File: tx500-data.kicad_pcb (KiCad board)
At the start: 2 copper layers, 80 x 50 mm, 27 parts, among them IC1 HS-100B, J1 USB_B, J2 CAT, J3 REM/DATA, J4 USB_A, U1 TUSB4041I, U2 FT232RL, Y1 24 MHz

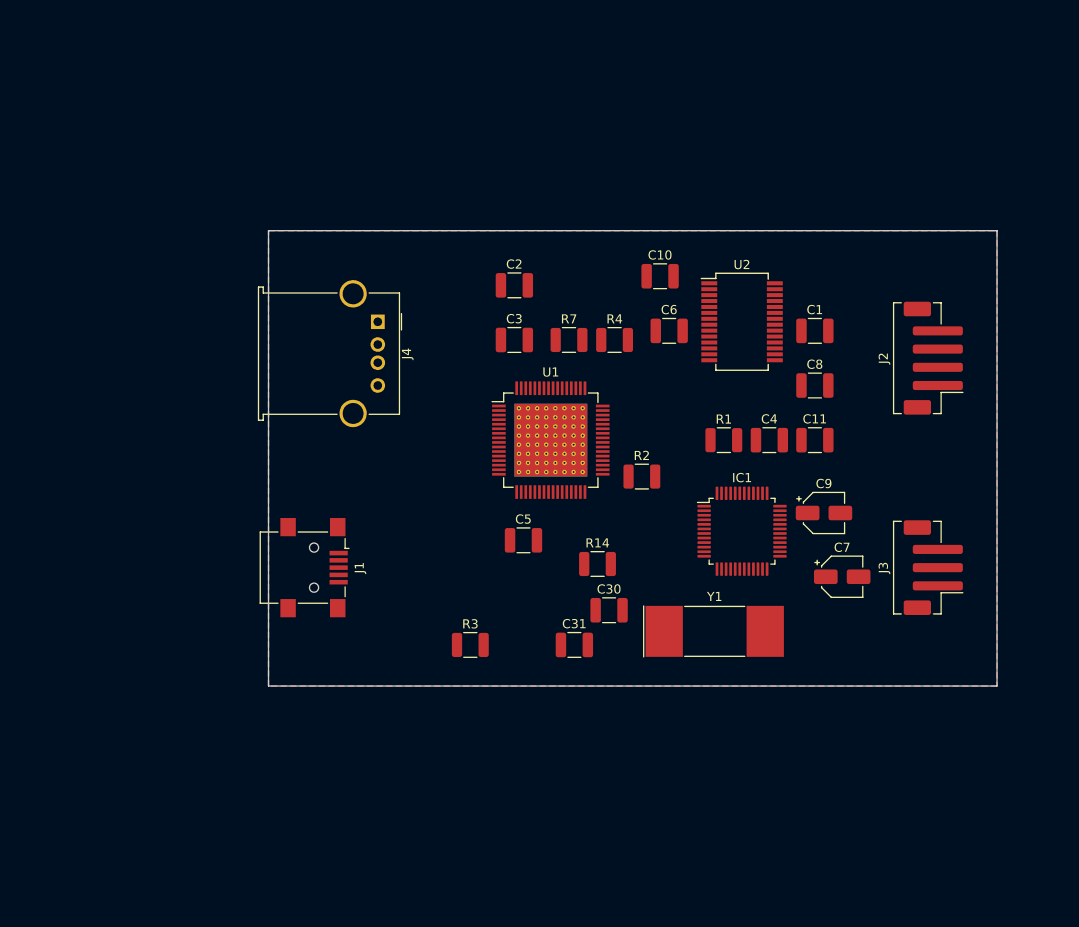
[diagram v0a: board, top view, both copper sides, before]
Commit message: Swap TUSB4041I for TUSB2036
The 4041 does more than I need it to, so use the 2036 instead.
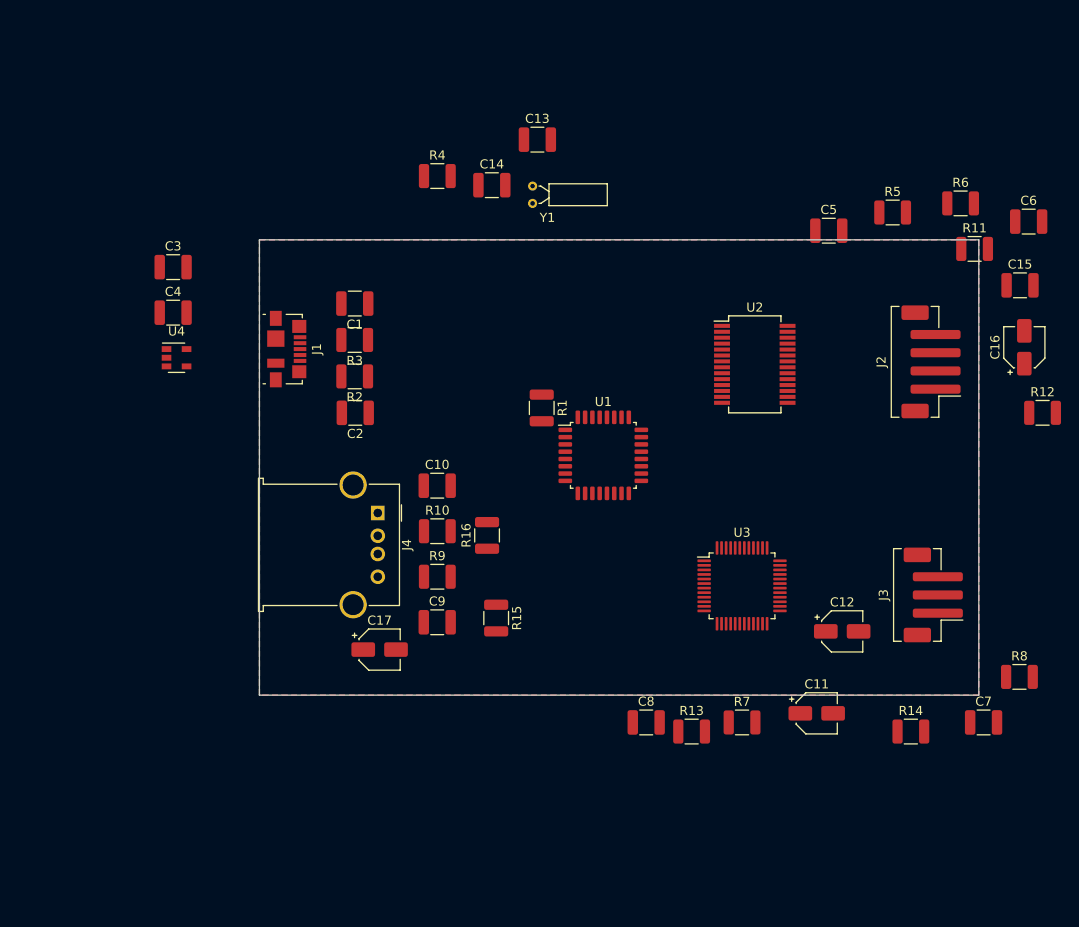
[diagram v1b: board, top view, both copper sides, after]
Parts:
- removed C30, C31: 18 pF, Capacitor_SMD:C_1210_3225Metric
- removed IC1: HS-100B, Package_QFP:LQFP-48_7x7mm_P0.5mm
- added C12: 10μF, Capacitor_SMD:CP_Elec_4x3, F.Cu at (178.0, 109.0)
- added C13: 27pF, Capacitor_SMD:C_1210_3225Metric, F.Cu at (144.5, 55.0)
- added C14: 27pF, Capacitor_SMD:C_1210_3225Metric, F.Cu at (139.5, 60.0)
- added C15: 100nF, Capacitor_SMD:C_1210_3225Metric, F.Cu at (197.5, 71.0)
- added C16: 100μF, Capacitor_SMD:CP_Elec_4x3, F.Cu at (198.0, 77.8)
- added C17: 100μF, Capacitor_SMD:CP_Elec_4x3, F.Cu at (127.2, 111.0)
- added R10: 27Ω, Resistor_SMD:R_1210_3225Metric, F.Cu at (133.5, 98.0)
- added R11: 15kΩ, Resistor_SMD:R_1210_3225Metric, F.Cu at (192.5, 67.0)
- added R12: 15kΩ, Resistor_SMD:R_1210_3225Metric, F.Cu at (200.0, 85.0)
- added R13: 15kΩ, Resistor_SMD:R_1210_3225Metric, F.Cu at (161.5, 120.0)
- added R15: 15kΩ, Resistor_SMD:R_1210_3225Metric, F.Cu at (140.0, 107.5)
- added R16: 15kΩ, Resistor_SMD:R_1210_3225Metric, F.Cu at (139.0, 98.5)
- added R5: 27Ω, Resistor_SMD:R_1210_3225Metric, F.Cu at (183.5, 63.0)
- added R6: 27Ω, Resistor_SMD:R_1210_3225Metric, F.Cu at (191.0, 62.0)
- added R8: 27Ω, Resistor_SMD:R_1210_3225Metric, F.Cu at (197.5, 114.0)
- added R9: 27Ω, Resistor_SMD:R_1210_3225Metric, F.Cu at (133.5, 103.0)
- added U3: HS-100B, Package_QFP:LQFP-48_7x7mm_P0.5mm, F.Cu at (167.0, 104.0)
- added U4: TPS76333, Package_TO_SOT_SMD:SOT-23-5, F.Cu at (104.9, 79.0)
- C1: value 10 μF -> 22pF
- C10, C8: value 100nF -> 22pF
- C11: value 10nF -> 100μF; footprint Capacitor_SMD:C_1210_3225Metric -> Capacitor_SMD:CP_Elec_4x3
- C2, C6: value 0.1μF -> 22pF
- C3: value 0.001μF -> 4.7μF
- C5: value 0.001μF -> 22pF
- C7: value 10.0 uF -> 22pF; footprint Capacitor_SMD:CP_Elec_4x3 -> Capacitor_SMD:C_1210_3225Metric
- C9: value 4.7μF -> 22pF; footprint Capacitor_SMD:CP_Elec_4x3 -> Capacitor_SMD:C_1210_3225Metric
- J1: footprint Connector_USB:USB_Mini-B_Lumberg_2486_01_Horizontal -> Connector_USB:USB_Micro-B_Molex_47346-0001
- R1: value 90.9 kΩ 1% -> 1.5kΩ
- R14: value 1 MΩ -> 15kΩ
- R2: value 10 kΩ 1% -> 27Ω
- R3: value 9.53 kΩ 1% -> 27Ω
- R4: value 10KΩ -> 1.5kΩ
- R7: value 1MΩ -> 27Ω
- U1: value TUSB4041I -> TUSB2036; footprint Package_QFP:HTQFP-64-1EP_10x10mm_P0.5mm_EP8x8mm_Mask4.4x4.4mm_ThermalVias -> Package_QFP:LQFP-32_7x7mm_P0.8mm
- Y1: value 24 MHz -> 6MHz; footprint Crystal:Crystal_SMD_SeikoEpson_MA505-2Pin_12.7x5.1mm -> Crystal:Crystal_DS26_D2.0mm_L6.0mm_Horizontal
- moved C4 67.0 mm to (104.5, 74.0)
- moved Y1 51.1 mm to (144.0, 62.0), turned to 90 degrees
- moved C1 50.6 mm to (124.5, 73.0), turned to 180 degrees
- moved C5 47.7 mm to (176.5, 65.0)
- moved R7 46.1 mm to (167.0, 119.0)
- moved C9 44.1 mm to (133.5, 108.0)
- moved C8 41.4 mm to (156.5, 119.0)
- moved C6 41.3 mm to (198.5, 64.0)
- moved R14 39.0 mm to (185.5, 120.0)
- moved C3 38.3 mm to (104.5, 69.0)
- moved R3 35.8 mm to (124.5, 77.0), turned to 180 degrees
- moved C10 33.6 mm to (133.5, 93.0)
- moved R2 33.4 mm to (124.5, 81.0), turned to 180 degrees
- moved C11 30.0 mm to (175.2, 118.0)
- moved R4 26.5 mm to (133.5, 59.0)
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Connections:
- C1 pad 1: VBUS -> /Upstream USB/USB_DM
- C2 pad 1: GNDPWR -> /Upstream USB/USB_DP
- C3 pad 1: GNDPWR -> VBUS
- C5 pad 1: GNDPWR -> Net-(C5-Pad1)
- C6 pad 1: GNDPWR -> Net-(C6-Pad1)
- C7 pad 2: Net-(C7-Pad2) -> GNDREF
- C8 pad 1: VBUS -> Net-(C8-Pad1)
- C9 pad 1: VBUS -> Net-(C9-Pad1)
- J1 pad 2: /Upstream USB/USB_DM -> Net-(J1-Pad2)
- J1 pad 3: /Upstream USB/USB_DP -> Net-(J1-Pad3)
- J1 pad 5: GNDPWR -> (no net)
- J2 pad 3: Net-(C10-Pad1) -> Net-(C15-Pad1)
- J3 pad 1: Net-(C7-Pad1) -> Net-(C12-Pad1)
- J4 pad 5: GNDPWR -> Net-(J4-Pad5)
- R1 pad 1: +1V1 -> Net-(R1-Pad1)
- R1 pad 2: VBUS -> /Upstream USB/USB_DP
- R14 pad 1: /Clock/XO -> /Audio Interface/USB_DM
- R14 pad 2: /Clock/XI -> GNDREF
- R2 pad 1: GNDREF -> /Upstream USB/USB_DP
- R2 pad 2: +1V1 -> Net-(J1-Pad3)
- R3 pad 1: GNDREF -> /Upstream USB/USB_DM
- R3 pad 2: Net-(R3-Pad2) -> Net-(J1-Pad2)
- R4 pad 1: GNDREF -> /Clock/XTAL2
- R4 pad 2: GNDPWR -> Net-(C14-Pad1)
- R7 pad 1: GNDREF -> /Audio Interface/USB_DP
- R7 pad 2: GNDPWR -> Net-(C7-Pad1)
- U1 pad 1: Net-(U1-Pad1) -> /Upstream USB/USB_DP
- U1 pad 10: Net-(U1-Pad10) -> (no net)
- U1 pad 11: Net-(U1-Pad11) -> Net-(C6-Pad1)
- U1 pad 12: Net-(U1-Pad12) -> Net-(C5-Pad1)
- U1 pad 13: Net-(U1-Pad13) -> (no net)
- U1 pad 14: Net-(U1-Pad14) -> (no net)
- U1 pad 15: Net-(U1-Pad15) -> Net-(C8-Pad1)
- U1 pad 16: +1V1 -> Net-(C7-Pad1)
- U1 pad 17: Net-(U1-Pad17) -> (no net)
- U1 pad 18: Net-(U1-Pad18) -> (no net)
- U1 pad 19: Net-(U1-Pad19) -> Net-(C10-Pad1)
- U1 pad 2: Net-(U1-Pad2) -> /Upstream USB/USB_DM
- U1 pad 20: Net-(U1-Pad2) -> Net-(C9-Pad1)
- U1 pad 21: /Upstream USB/USB_DP -> (no net)
- U1 pad 22: /Upstream USB/USB_DM -> GNDREF
- U1 pad 24: Net-(U1-Pad24) -> GNDREF
- U1 pad 25: Net-(U1-Pad19) -> /Upstream USB/US_33
- U1 pad 26: Net-(U1-Pad26) -> Net-(U1-Pad23)
- U1 pad 27: Net-(U1-Pad27) -> Net-(R1-Pad1)
- U1 pad 28: Net-(U1-Pad28) -> GNDREF
- U1 pad 29: /Clock/XO -> /Clock/XTAL2
- U1 pad 3: Net-(U1-Pad3) -> /Upstream USB/US_33
- U1 pad 30: /Clock/XI -> /Clock/XTAL1
- U1 pad 31: Net-(U1-Pad2) -> GNDREF
- U1 pad 32: Net-(R3-Pad2) -> (no net)
- U1 pad 4: Net-(U1-Pad4) -> (no net)
- U1 pad 5: Net-(U1-Pad5) -> (no net)
- U1 pad 6: Net-(U1-Pad6) -> GNDREF
- U1 pad 7: Net-(U1-Pad7) -> GNDREF
- U1 pad 8: Net-(U1-Pad8) -> Net-(U1-Pad23)
- U1 pad 9: Net-(U1-Pad9) -> (no net)
- U2 pad 10: Net-(U2-Pad10) -> (no net)
- U2 pad 11: Net-(U2-Pad11) -> (no net)
- U2 pad 12: Net-(U2-Pad12) -> (no net)
- U2 pad 13: Net-(U2-Pad13) -> (no net)
- U2 pad 14: Net-(U2-Pad14) -> (no net)
- U2 pad 17: Net-(C10-Pad1) -> Net-(C15-Pad1)
- U2 pad 19: Net-(U2-Pad19) -> (no net)
- U2 pad 2: Net-(U2-Pad2) -> (no net)
- U2 pad 22: Net-(U2-Pad22) -> (no net)
- U2 pad 23: Net-(U2-Pad23) -> (no net)
- U2 pad 27: Net-(U2-Pad27) -> (no net)
- U2 pad 28: Net-(U2-Pad28) -> (no net)
- U2 pad 3: Net-(U2-Pad3) -> (no net)
- U2 pad 4: Net-(C10-Pad1) -> Net-(C15-Pad1)
- U2 pad 6: Net-(U2-Pad6) -> (no net)
- U2 pad 9: Net-(U2-Pad9) -> (no net)
- Y1 pad 1: /Clock/XI -> /Clock/XTAL1
- Y1 pad 2: /Clock/XO -> Net-(C14-Pad1)
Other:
- board size 80 x 50 mm -> 79 x 50 mm

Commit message: Add BOM and clarify some footprints
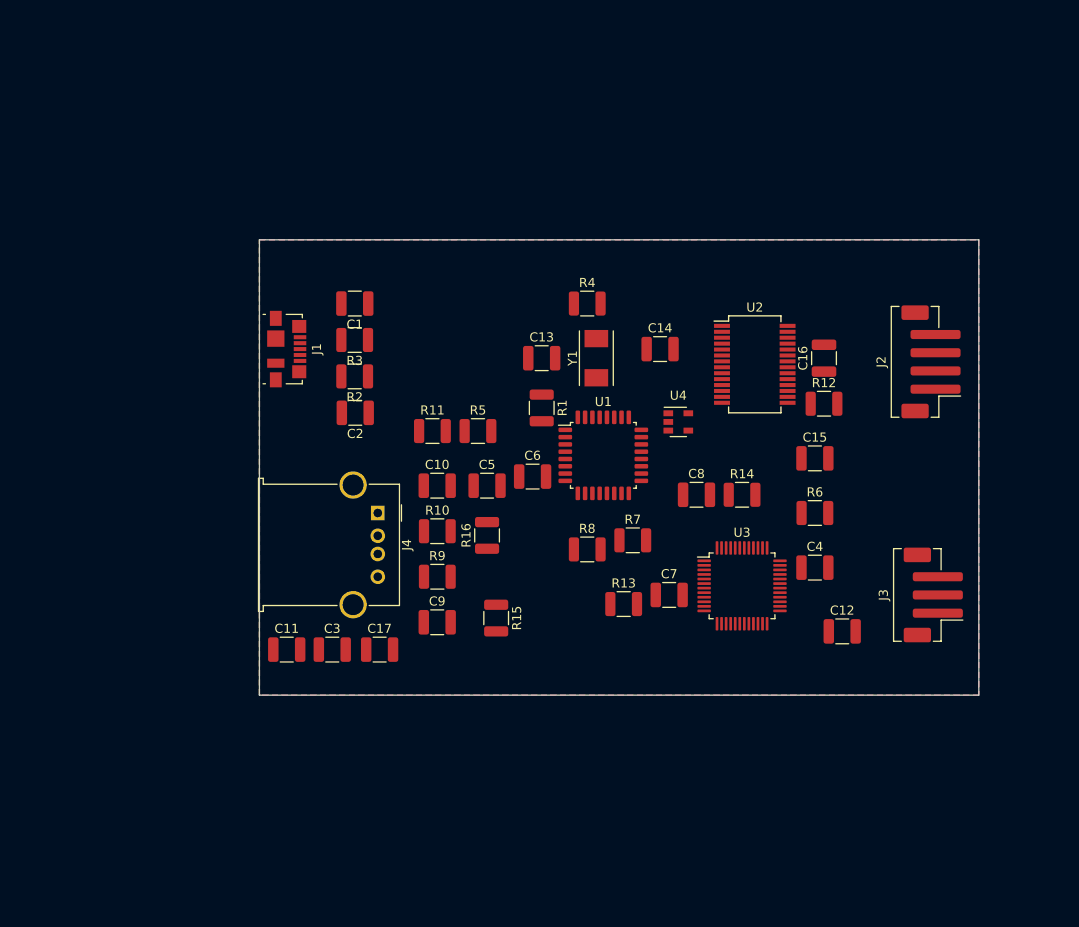
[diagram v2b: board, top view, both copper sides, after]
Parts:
- C11, C12, C16, C17: footprint Capacitor_SMD:CP_Elec_4x3 -> Capacitor_SMD:C_1210_3225Metric
- C15: value 100nF -> 0.1μF
- Y1: footprint Crystal:Crystal_DS26_D2.0mm_L6.0mm_Horizontal -> Crystal:Crystal_SMD_Abracon_ABM7-2Pin_6.0x3.5mm
- moved C4 75.8 mm to (175.0, 102.0)
- moved R11 62.8 mm to (133.0, 87.0)
- moved C6 61.2 mm to (144.0, 92.0)
- moved C11 58.6 mm to (117.0, 111.0)
- moved U4 55.5 mm to (160.0, 86.0)
- moved R5 51.5 mm to (138.0, 87.0)
- moved R8 49.5 mm to (150.0, 100.0)
- moved C5 46.8 mm to (139.0, 93.0)
- moved C3 45.5 mm to (122.0, 111.0)
- moved R6 37.6 mm to (175.0, 96.0)
- moved C7 37.3 mm to (159.0, 105.0)
- moved R14 31.9 mm to (167.0, 94.0)
- moved C15 29.5 mm to (175.0, 90.0)
- moved C14 25.8 mm to (158.0, 78.0)
- moved C8 25.6 mm to (162.0, 94.0)
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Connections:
- J1 pad 5: (no net) -> Net-(J1-Pad5)
- U1 pad 10: (no net) -> Net-(U1-Pad10)
- U1 pad 13: (no net) -> Net-(U1-Pad13)
- U1 pad 14: (no net) -> Net-(U1-Pad14)
- U1 pad 17: (no net) -> Net-(U1-Pad17)
- U1 pad 18: (no net) -> Net-(U1-Pad18)
- U1 pad 21: (no net) -> Net-(U1-Pad21)
- U1 pad 32: (no net) -> Net-(U1-Pad32)
- U1 pad 4: (no net) -> Net-(U1-Pad4)
- U1 pad 5: (no net) -> Net-(U1-Pad5)
- U1 pad 9: (no net) -> Net-(U1-Pad9)
- U2 pad 10: (no net) -> Net-(U2-Pad10)
- U2 pad 11: (no net) -> Net-(U2-Pad11)
- U2 pad 12: (no net) -> Net-(U2-Pad12)
- U2 pad 13: (no net) -> Net-(U2-Pad13)
- U2 pad 14: (no net) -> Net-(U2-Pad14)
- U2 pad 19: (no net) -> Net-(U2-Pad19)
- U2 pad 2: (no net) -> Net-(U2-Pad2)
- U2 pad 22: (no net) -> Net-(U2-Pad22)
- U2 pad 23: (no net) -> Net-(U2-Pad23)
- U2 pad 27: (no net) -> Net-(U2-Pad27)
- U2 pad 28: (no net) -> Net-(U2-Pad28)
- U2 pad 3: (no net) -> Net-(U2-Pad3)
- U2 pad 6: (no net) -> Net-(U2-Pad6)
- U2 pad 9: (no net) -> Net-(U2-Pad9)
- U3 pad 1: (no net) -> Net-(U3-Pad1)
- U3 pad 11: (no net) -> Net-(U3-Pad11)
- U3 pad 13: (no net) -> Net-(U3-Pad13)
- U3 pad 14: (no net) -> Net-(U3-Pad14)
- U3 pad 15: (no net) -> Net-(U3-Pad15)
- U3 pad 16: (no net) -> Net-(U3-Pad16)
- U3 pad 17: (no net) -> Net-(U3-Pad17)
- U3 pad 18: (no net) -> Net-(U3-Pad18)
- U3 pad 19: (no net) -> Net-(U3-Pad19)
- U3 pad 2: (no net) -> Net-(U3-Pad2)
- U3 pad 21: (no net) -> Net-(U3-Pad21)
- U3 pad 22: (no net) -> Net-(U3-Pad22)
- U3 pad 23: (no net) -> Net-(U3-Pad23)
- U3 pad 24: (no net) -> Net-(U3-Pad24)
- U3 pad 26: (no net) -> Net-(U3-Pad26)
- U3 pad 27: (no net) -> Net-(U3-Pad27)
- U3 pad 3: (no net) -> Net-(U3-Pad3)
- U3 pad 31: (no net) -> Net-(U3-Pad31)
- U3 pad 37: (no net) -> Net-(U3-Pad37)
- U3 pad 38: (no net) -> Net-(U3-Pad38)
- U3 pad 39: (no net) -> Net-(U3-Pad39)
- U3 pad 4: (no net) -> Net-(U3-Pad4)
- U3 pad 41: (no net) -> Net-(U3-Pad41)
- U3 pad 42: (no net) -> Net-(U3-Pad42)
- U3 pad 45: (no net) -> Net-(U3-Pad45)
- U3 pad 46: (no net) -> Net-(U3-Pad46)
- U3 pad 47: (no net) -> Net-(U3-Pad47)
- U3 pad 48: (no net) -> Net-(U3-Pad48)
- U3 pad 5: (no net) -> Net-(U3-Pad5)
- U3 pad 7: (no net) -> Net-(U3-Pad7)
- U3 pad 9: (no net) -> Net-(U3-Pad9)
- U4 pad 3: (no net) -> Net-(U4-Pad3)
- U4 pad 4: (no net) -> Net-(U4-Pad4)

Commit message: Add a 15mm buffer for the GX12 bulkhead connectors
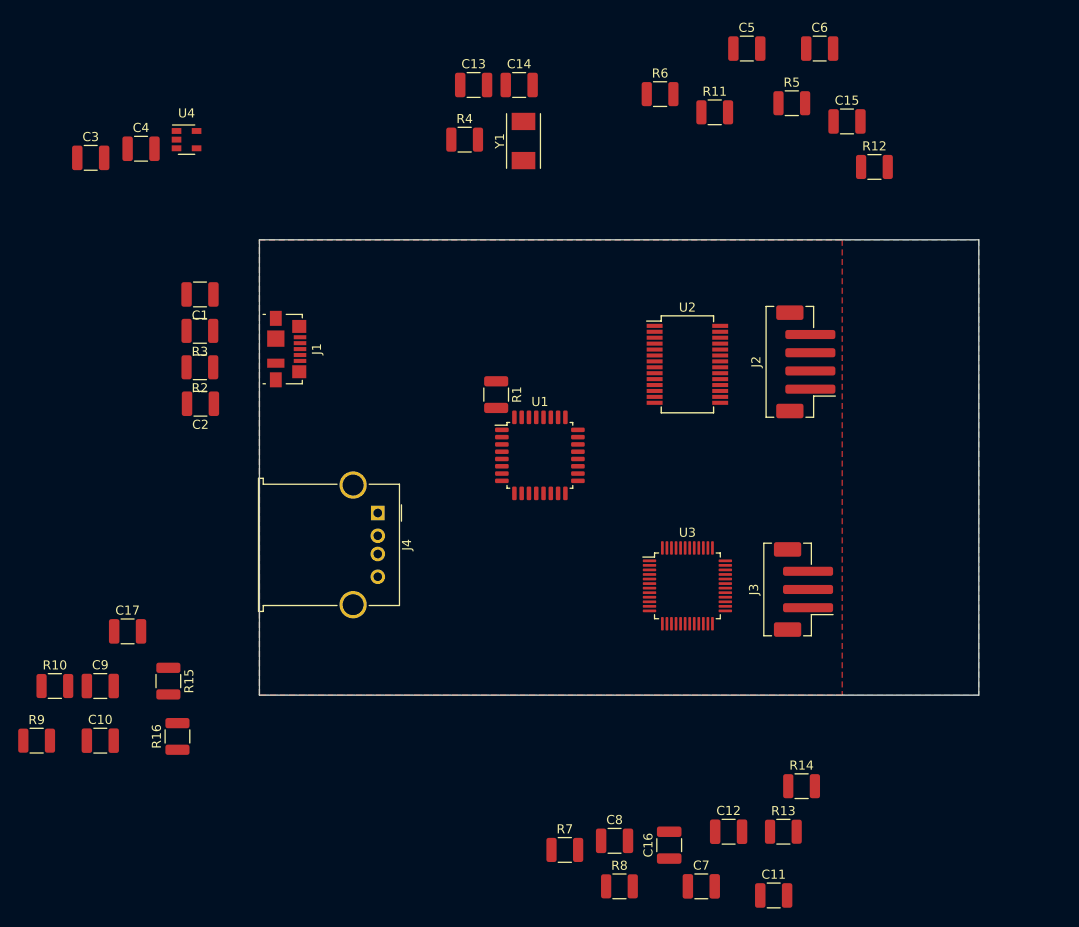
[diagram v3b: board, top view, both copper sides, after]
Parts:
- moved C4 87.1 mm to (101.0, 56.0)
- moved U4 62.3 mm to (106.0, 55.0)
- moved C3 60.2 mm to (95.5, 57.0)
- moved C11 59.9 mm to (170.5, 138.0)
- moved C6 56.6 mm to (175.5, 45.0)
- moved C16 56.1 mm to (159.0, 132.5)
- moved C5 55.8 mm to (167.5, 45.0)
- moved R5 49.8 mm to (172.5, 51.0)
- moved R6 49.0 mm to (158.0, 50.0)
- moved R9 47.5 mm to (89.5, 121.0)
- moved R11 46.8 mm to (164.0, 52.0)
- moved C10 46.4 mm to (96.5, 121.0)
- moved R10 45.3 mm to (91.5, 115.0)
- moved R16 40.5 mm to (105.0, 120.5)
- moved C8 39.1 mm to (153.0, 132.0)
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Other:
- board text added: "Leave 15mm for GX12 bulkhead connectors"
